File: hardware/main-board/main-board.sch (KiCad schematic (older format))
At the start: 84 parts, among them J1 USB_B_Micro, J2 DNI, J3 Display Connector, J4 Conn_01x02, SW1 SW_Push, SW2 SW_Push, SW3 SW_Push, SW4 SW_Push, SW5 SW_Detect, SW6 SW_Boot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

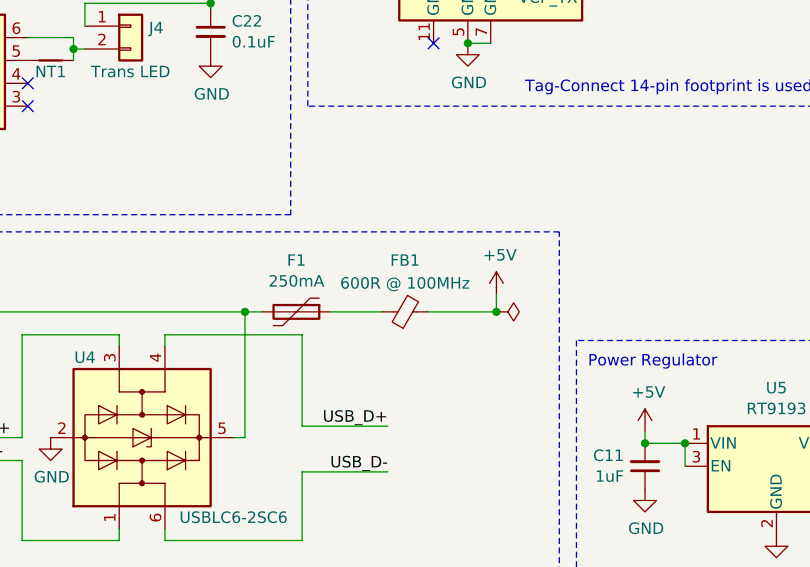
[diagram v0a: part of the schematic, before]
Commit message: Fixed ferrite bead component description
Two identical parts should have identical descriptions to make the BOM
data nicer.
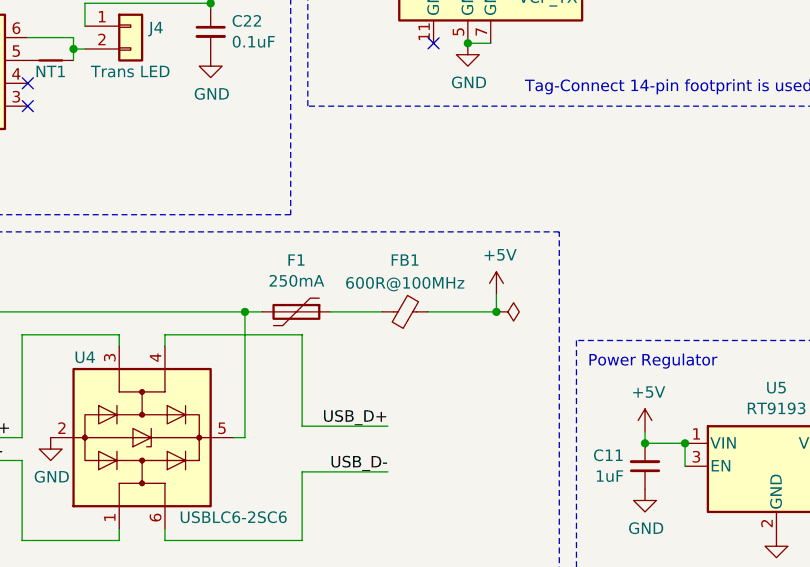
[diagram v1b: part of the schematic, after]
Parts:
- FB1: value 600R @ 100MHz -> 600R@100MHz
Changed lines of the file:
@@
 P 3375 6725
 F 0 "FB1" V 3150 6725 50  0000 C CNN
-F 1 "600R @ 100MHz" V 3250 6725 50  0000 C CNN
+F 1 "600R@100MHz" V 3250 6725 50  0000 C CNN
 F 2 "Inductor_SMD:L_0603_1608Metric" V 3305 6725 50  0001 C CNN
 F 3 "https://product.tdk.com/en/system/files?file=dam/doc/product/emc/emc/beads/catalog/beads_commercial_signal_mmz1608_en.pdf" H 3375 6725 50  0001 C CNN

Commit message: Update LED footprints for thermal properties
Fixes naming convention of thermally-enhanced LED footprints to be
closer to the KiCad convention, and separates into two versions. One
with thermal vias and one without.

Updated transmission board metadata to referene the correct new
footprint name.

Updated main board to use the new version of the new footprint without
thermal vias.

Fixes #22
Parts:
- D1, D2, D3, D4: footprint lib_fp:LED_WL-SWTP-3022 -> lib_fp:LED_WL-SWTP-3022-1MP
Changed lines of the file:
@@
 F 0 "D1" H 2150 4375 50  0000 C CNN
 F 1 "LED" H 2143 4401 50  0001 C CNN
-F 2 "lib_fp:LED_WL-SWTP-3022" H 2150 4275 50  0001 C CNN
+F 2 "lib_fp:LED_WL-SWTP-3022-1MP" H 2150 4275 50  0001 C CNN
 F 3 "https://katalog.we-online.de/led/datasheet/158302250.pdf" H 2150 4275 50  0001 C CNN
 F 4 "LED WL-SWTP COOL WHT 5000K 2SMD" H 2150 4275 50  0001 C CNN "Description"
@@
 F 0 "D2" H 2150 4625 50  0000 C CNN
 F 1 "LED" H 2143 4651 50  0001 C CNN
-F 2 "lib_fp:LED_WL-SWTP-3022" H 2150 4525 50  0001 C CNN
+F 2 "lib_fp:LED_WL-SWTP-3022-1MP" H 2150 4525 50  0001 C CNN
 F 3 "https://katalog.we-online.de/led/datasheet/158302250.pdf" H 2150 4525 50  0001 C CNN
 F 4 "LED WL-SWTP COOL WHT 5000K 2SMD" H 2150 4525 50  0001 C CNN "Description"
@@
 F 0 "D3" H 2150 4875 50  0000 C CNN
 F 1 "LED" H 2143 4901 50  0001 C CNN
-F 2 "lib_fp:LED_WL-SWTP-3022" H 2150 4775 50  0001 C CNN
+F 2 "lib_fp:LED_WL-SWTP-3022-1MP" H 2150 4775 50  0001 C CNN
 F 3 "https://katalog.we-online.de/led/datasheet/158302250.pdf" H 2150 4775 50  0001 C CNN
 F 4 "LED WL-SWTP COOL WHT 5000K 2SMD" H 2150 4775 50  0001 C CNN "Description"
@@
 F 0 "D4" H 2150 5125 50  0000 C CNN
 F 1 "LED" H 2143 5151 50  0001 C CNN
-F 2 "lib_fp:LED_WL-SWTP-3022" H 2150 5025 50  0001 C CNN
+F 2 "lib_fp:LED_WL-SWTP-3022-1MP" H 2150 5025 50  0001 C CNN
 F 3 "https://katalog.we-online.de/led/datasheet/158302250.pdf" H 2150 5025 50  0001 C CNN
 F 4 "LED WL-SWTP COOL WHT 5000K 2SMD" H 2150 5025 50  0001 C CNN "Description"

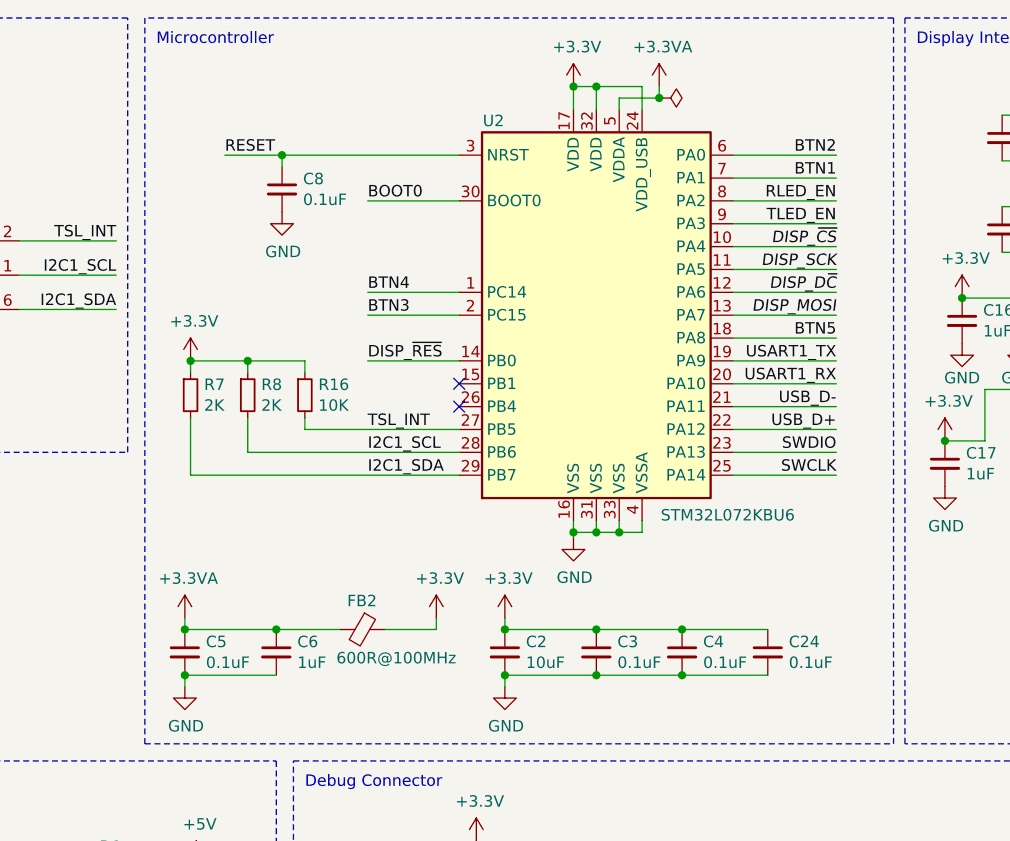
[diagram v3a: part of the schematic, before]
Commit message: Change MCU on schematic
This changes the MCU on the schematic from STM32L072KBU6 to STM32L072KZT6.

The new MCU has more GPIO pins, which are not needed and thus marked as
such. It also has one less power pin, so bypass capacitor C24 has been
removed.

Refs #21
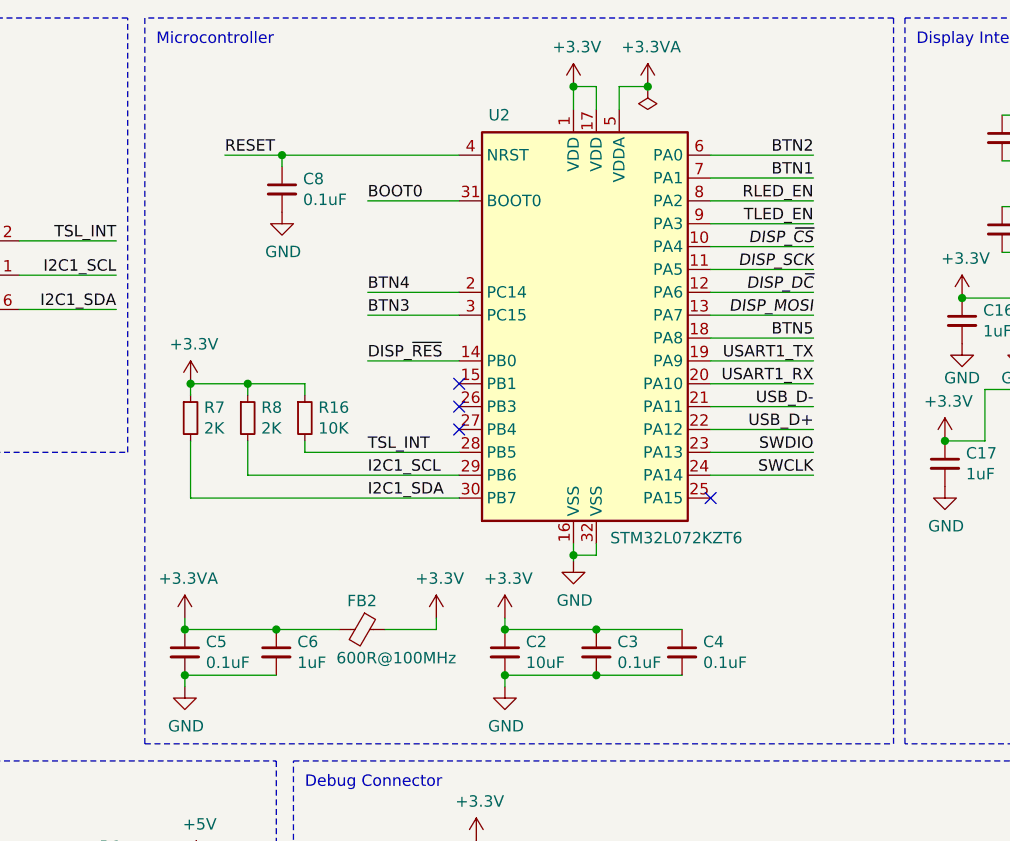
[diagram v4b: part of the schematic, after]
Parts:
- removed C24: 0.1uF, Capacitor_SMD:C_0603_1608Metric, symbol Device:C_Small
- removed U2: STM32L072KBU6, Package_DFN_QFN:QFN-32-1EP_5x5mm_P0.5mm_EP3.45x3.45mm, symbol MCU_ST_STM32L0:STM32L072KBUx
- added U2: STM32L072KZT6, Package_QFP:LQFP-32_7x7mm_P0.8mm, symbol MCU_ST_STM32L0:STM32L072KZTx
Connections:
- net +3.3VA: now also U2.5 (VDDA)
- net +3V3: now also U2.1 (VDD), U2.17 (VDD)
- net BOOT0: now also U2.31 (BOOT0)
- net BTN1: now also U2.7 (PA1)
- net BTN2: now also U2.6 (PA0)
- net BTN3: now also U2.3 (PC15)
- net BTN4: now also U2.2 (PC14)
- net BTN5: now also U2.18 (PA8)
- net DISP_D~C: now also U2.12 (PA6)
- net DISP_MOSI: now also U2.13 (PA7)
- net DISP_SCK: now also U2.11 (PA5)
- net DISP_~CS: now also U2.10 (PA4)
- net DISP_~RES: now also U2.14 (PB0)
- net GND: now also U2.16 (VSS), U2.32 (VSS)
- net I2C1_SCL: now also U2.29 (PB6)
- net I2C1_SDA: now also U2.30 (PB7)
- net RESET: now also U2.4 (NRST)
- net RLED_EN: now also U2.8 (PA2)
- net SWCLK: now also U2.24 (PA14)
- net SWDIO: now also U2.23 (PA13)
- net TLED_EN: now also U2.9 (PA3)
- net TSL_INT: now also U2.28 (PB5)
- net USART1_RX: now also U2.20 (PA10)
- net USART1_TX: now also U2.19 (PA9)
- net USB_D+: now also U2.22 (PA12)
- net USB_D-: now also U2.21 (PA11)
- no-connect marks 11 -> 13
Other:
- moved on the sheet: R16, R7, R8

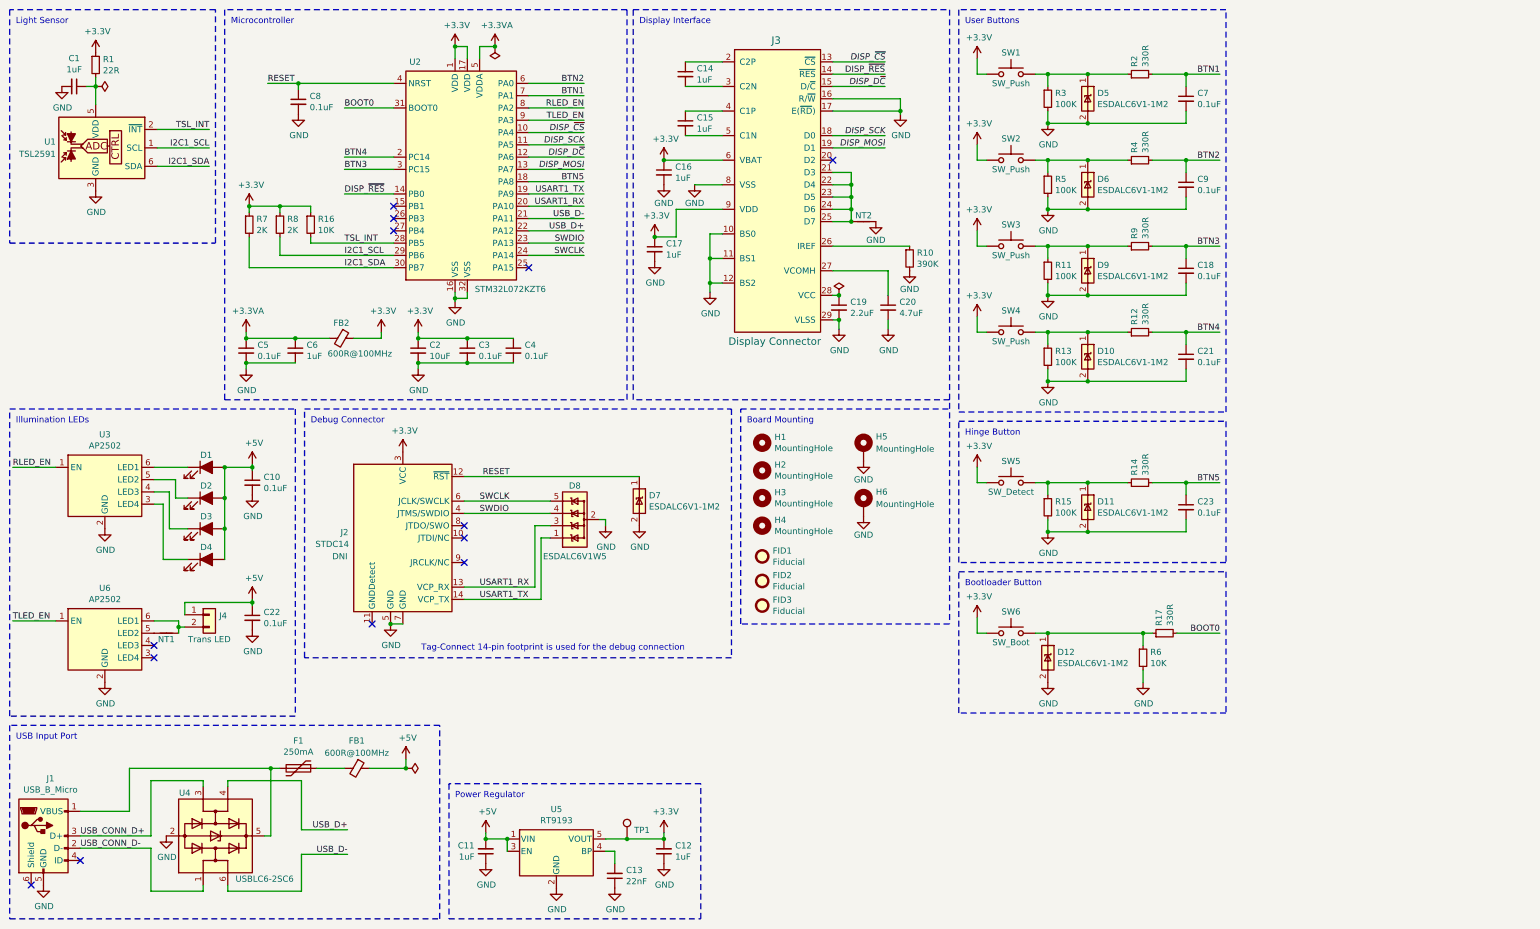
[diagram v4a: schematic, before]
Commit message: Added USB-C connector to main board schematic
- Switched the USB Micro-B connector to a USB 2.0 capable USB-C connector
- Implemented connections based on AN5225 guidance, which just involves
  connecting the D+/D- pins together and adding CC1/CC2 pull-down
  resistors. This is the simplest way to implement it.
- Increased sheet size from US Letter to US Legal to avoid the the need
  to break the schematic into multiple pages for just this one change,
  as the USB-C connector symbol is much bigger
- Linked the connector to the TVS diode and power filtering components
  via labels, to avoid the schematic getting too messy in that area.

Refs #18
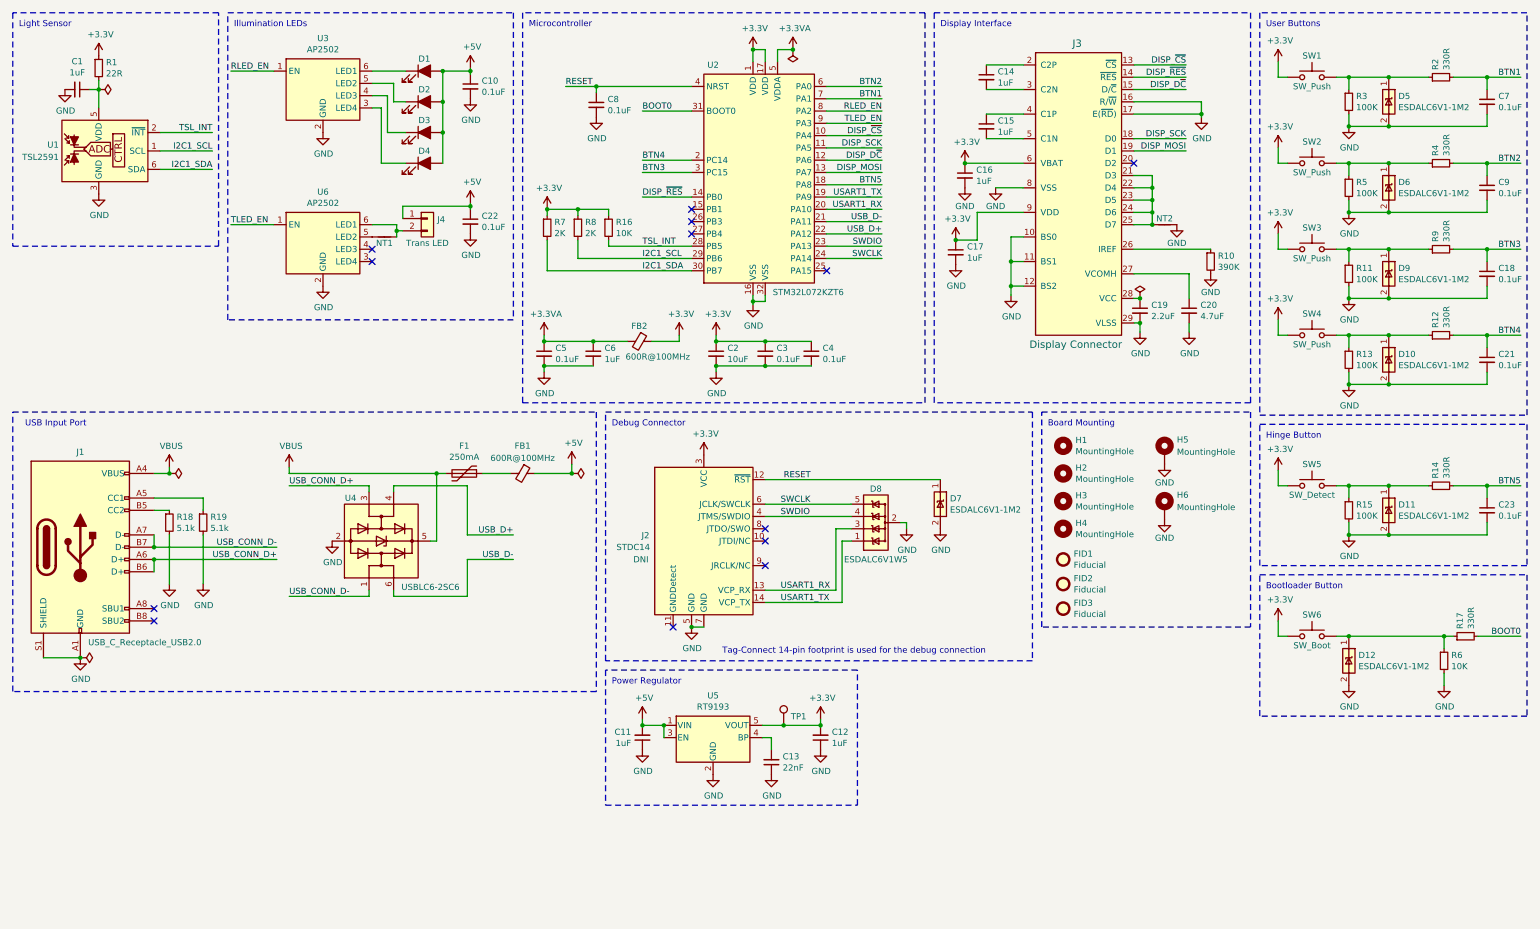
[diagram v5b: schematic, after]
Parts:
- removed J1: USB_B_Micro, Connector_USB:USB_Micro-B_Amphenol_10118194_Horizontal, symbol Connector:USB_B_Micro
- added J1: USB_C_Receptacle_USB2.0, Connector_USB:USB_C_Receptacle_Palconn_UTC16-G, symbol Connector:USB_C_Receptacle_USB2.0
- added R18, R19: 5.1k, Resistor_SMD:R_0603_1608Metric, symbol Device:R_Small
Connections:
- net GND: now also J1.A1 (GND), J1.A12 (GND), J1.B1 (GND), J1.B12 (GND), J1.S1 (SHIELD), R18.2, R19.2
- net USB_CONN_D+: now also J1.A6 (D+), J1.B6 (D+)
- net USB_CONN_D-: now also J1.A7 (D-), J1.B7 (D-)
- net VBUS: now reaches F1.2, U4.5 (VBUS)
- net VBUS: now also J1.A4 (VBUS), J1.A9 (VBUS), J1.B4 (VBUS), J1.B9 (VBUS)
- new net: J1.A5 (CC1), R19.1
- new net: J1.B5 (CC2), R18.1
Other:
- moved on the sheet: C1, C10, C11, C12, C13, C14, C15, C16, C17, C18, C19, C2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

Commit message: Updated footprints for LQFP-32 and USB-C connector
LQFP-32 footprint is based on the stock footprint, modified according to
the recommended footprint in ST's datasheet. This reduces the length of
the pads under the leads, which may help reduce bridging.

USB-C footprint is based on the stock Palcon footprint, modified
according to the GCT datasheet. This is several very minor changes, that
might not even make much of a difference.
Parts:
- J1: footprint Connector_USB:USB_C_Receptacle_Palconn_UTC16-G -> lib_fp:USB_C_Receptacle_GCT_USB4105
- U2: footprint Package_QFP:LQFP-32_7x7mm_P0.8mm -> lib_fp:ST_LQFP32
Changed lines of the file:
@@
 F 0 "U2" H 6275 2750 50  0000 C CNN
 F 1 "STM32L072KZT6" H 7050 900 50  0000 C CNN
-F 2 "Package_QFP:LQFP-32_7x7mm_P0.8mm" H 6200 975 50  0001 R CNN
+F 2 "lib_fp:ST_LQFP32" H 6200 975 50  0001 R CNN
 F 3 "http://www.st.com/st-web-ui/static/active/en/resource/technical/document/datasheet/DM00141133.pdf" H 6700 1875 50  0001 C CNN
 F 4 "IC MCU 32BIT 192KB FLASH 32LQFP" H 6700 1875 50  0001 C CNN "Description"
@@
 F 0 "J1" H 1125 5700 50  0000 C CNN
 F 1 "USB_C_Receptacle_USB2.0" H 1650 4150 50  0000 C CNN
-F 2 "Connector_USB:USB_C_Receptacle_Palconn_UTC16-G" H 1275 4925 50  0001 C CNN
+F 2 "lib_fp:USB_C_Receptacle_GCT_USB4105" H 1275 4925 50  0001 C CNN
 F 3 "https://gct.co/files/specs/usb4105-spec.pdf" H 1275 4925 50  0001 C CNN
 F 4 "CONN RCP USB2.0 TYP C 24P SMD RA" H 1125 4925 50  0001 C CNN "Description"
